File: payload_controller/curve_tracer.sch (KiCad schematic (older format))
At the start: 28 parts, among them U10 OPA2387, U12 ADS131M04IPWR, U13 INA190A4IDDFR, U31 LT6654AMPS6-1.25

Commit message: Continuing layout
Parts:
- removed U10: OPA2387, Package_SON:WSON-8-1EP_2x2mm_P0.5mm_EP0.9x1.6mm, symbol OPA2387:OPA2387
- added U10: OPA2387, Package_SON:WSON-8-1EP_2x2mm_P0.5mm_EP0.9x1.6mm, symbol OPA2387:OPA2387
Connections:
- net +3V3: now also U10.8
- net -3V3: now also U10.4
- net at R23.2: now also U10.1, U10.2 (-)
- net at R25.1: now also U10.3 (+)
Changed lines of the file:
@@
 $EndComp
-$Comp
-L OPA2387:OPA2387 U10
-U 2 1 6382B343
-P 7750 4550
-F 0 "U10" H 8000 4850 50  0000 C CNN
-F 1 "OPA2387" H 8100 4750 50  0000 C CNN
-F 2 "Package_SON:WSON-8-1EP_2x2mm_P0.5mm_EP0.9x1.6mm" H 8150 4750 50  0001 C CNN
-F 3 "" H 8150 4750 50  0001 C CNN
-	2    7750 4550
-	-1   0    0    -1
-$EndComp
-Connection ~ 7250 4550
 $Comp
 L power:-3V3 #PWR0151
 U 1 1 63853834
-P 8200 4750
-F 0 "#PWR0151" H 8200 4850 50  0001 C CNN
-F 1 "-3V3" H 8215 4923 50  0000 C CNN
-F 2 "" H 8200 4750 50  0001 C CNN
-F 3 "" H 8200 4750 50  0001 C CNN
-	1    8200 4750
+P 7650 4850
+F 0 "#PWR0151" H 7650 4950 50  0001 C CNN
+F 1 "-3V3" H 7665 5023 50  0000 C CNN
+F 2 "" H 7650 4850 50  0001 C CNN
+F 3 "" H 7650 4850 50  0001 C CNN
+	1    7650 4850
 	-1   0    0    1
 $EndComp
-Wire Wire Line
-	8000 4550 8200 4550
-Wire Wire Line
-	8200 4550 8200 4750
+$Comp
+L power:+3V3 #PWR0135
+U 1 1 63AD679A
+P 7650 4250
+F 0 "#PWR0135" H 7650 4100 50  0001 C CNN
+F 1 "+3V3" H 7665 4423 50  0000 C CNN
+F 2 "" H 7650 4250 50  0001 C CNN
+F 3 "" H 7650 4250 50  0001 C CNN
+	1    7650 4250
+	1    0    0    -1
+$EndComp
+$Comp
+L OPA2387:OPA2387 U?
+U 1 1 63AD4C17
+P 7750 4550
+AR Path="/635FEB2F/63AD4C17" Ref="U?"  Part="1"
+AR Path="/63C503EE/63AD4C17" Ref="U10"  Part="1"
+F 0 "U10" H 8100 4850 50  0000 R CNN
+F 1 "OPA2387" H 8300 4750 50  0000 R CNN
+F 2 "Package_SON:WSON-8-1EP_2x2mm_P0.5mm_EP0.9x1.6mm" H 8150 4750 50  0001 C CNN
+F 3 "" H 8150 4750 50  0001 C CNN
+	1    7750 4550
+	-1   0    0    -1
+$EndComp
 $EndSCHEMATC

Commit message: Continuing payload design
- Add OR gate for reverse bias
- Add GaAs panel connectors
- Add 3D models
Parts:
- added TP1: Current Test, Connector_PinHeader_2.54mm:PinHeader_1x02_P2.54mm_Vertical, symbol Connector:TestPoint_2Pole
- added TP2: Voltage Test+, Connector_PinHeader_2.54mm:PinHeader_1x01_P2.54mm_Vertical, symbol Connector:TestPoint
- added TP3: Voltage Test-, Connector_PinHeader_2.54mm:PinHeader_1x01_P2.54mm_Vertical, symbol Connector:TestPoint
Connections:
- net GND: now also TP3.1
- net PANEL_VOLTAGE: now also TP1.1; no longer R24.2, U13.7 (IN+)
- net at R25.2, R26.1, R27.2: now also TP2.1
- new net: R24.2, TP1.2, U13.7 (IN+)
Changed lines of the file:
@@
 Wire Wire Line
 	7450 2250 7450 2650
-Connection ~ 7450 2250
 Wire Wire Line
 	8450 2250 8450 4100
 Wire Wire Line
-	3300 2250 7450 2250
-Wire Wire Line
-	8450 5150 8450 4700
+	8450 5150 8450 4850
 Wire Wire Line
 	6400 4550 6950 4550
@@
 	-1   0    0    -1
 $EndComp
+$Comp
+L Connector:TestPoint TP?
+U 1 1 63A754DC
+P 8750 4400
+AR Path="/635FE71D/63A754DC" Ref="TP?"  Part="1"
+AR Path="/63C503EE/63A754DC" Ref="TP2"  Part="1"
+F 0 "TP2" V 8704 4588 50  0000 L CNN
+F 1 "Voltage Test+" V 8795 4588 50  0000 L CNN
+F 2 "Connector_PinHeader_2.54mm:PinHeader_1x01_P2.54mm_Vertical" H 8950 4400 50  0001 C CNN
+F 3 "~" H 8950 4400 50  0001 C CNN
+	1    8750 4400
+	0    1    1    0
+$EndComp
+Wire Wire Line
+	8750 4400 8450 4400
+$Comp
+L Connector:TestPoint_2Pole TP1
+U 1 1 63A77455
+P 6450 2250
+F 0 "TP1" H 6450 2445 50  0000 C CNN
+F 1 "Current Test" H 6450 2354 50  0000 C CNN
+F 2 "Connector_PinHeader_2.54mm:PinHeader_1x02_P2.54mm_Vertical" H 6450 2250 50  0001 C CNN
+F 3 "~" H 6450 2250 50  0001 C CNN
+	1    6450 2250
+	1    0    0    -1
+$EndComp
+Wire Wire Line
+	6650 2250 7450 2250
+Connection ~ 7450 2250
+Wire Wire Line
+	6250 2250 3300 2250
+$Comp
+L Connector:TestPoint TP?
+U 1 1 63A8A109
+P 8750 4850
+AR Path="/635FE71D/63A8A109" Ref="TP?"  Part="1"
+AR Path="/63C503EE/63A8A109" Ref="TP3"  Part="1"
+F 0 "TP3" V 8704 5038 50  0000 L CNN
+F 1 "Voltage Test-" V 8795 5038 50  0000 L CNN
+F 2 "Connector_PinHeader_2.54mm:PinHeader_1x01_P2.54mm_Vertical" H 8950 4850 50  0001 C CNN
+F 3 "~" H 8950 4850 50  0001 C CNN
+	1    8750 4850
+	0    1    1    0
+$EndComp
+Wire Wire Line
+	8750 4850 8450 4850
+Connection ~ 8450 4850
+Wire Wire Line
+	8450 4850 8450 4700
 $EndSCHEMATC

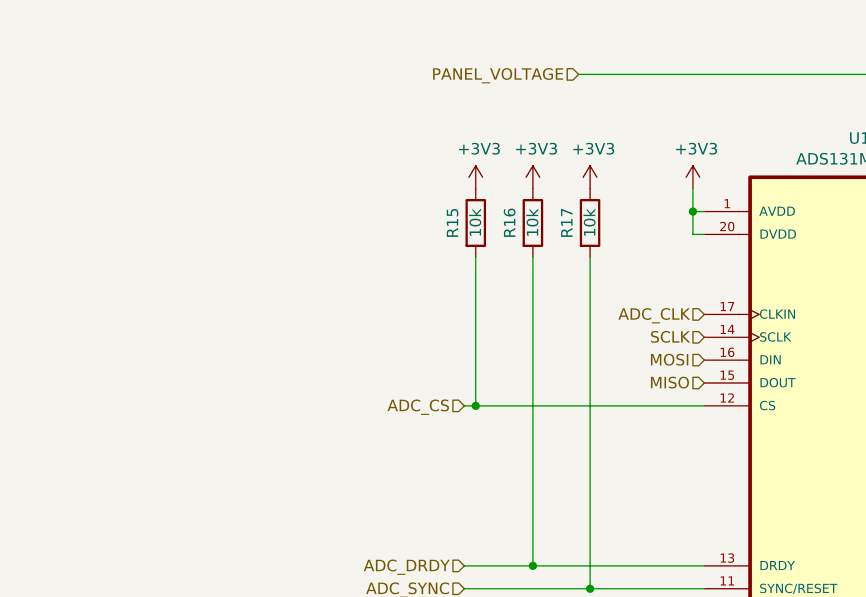
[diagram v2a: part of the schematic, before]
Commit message: Completed routing
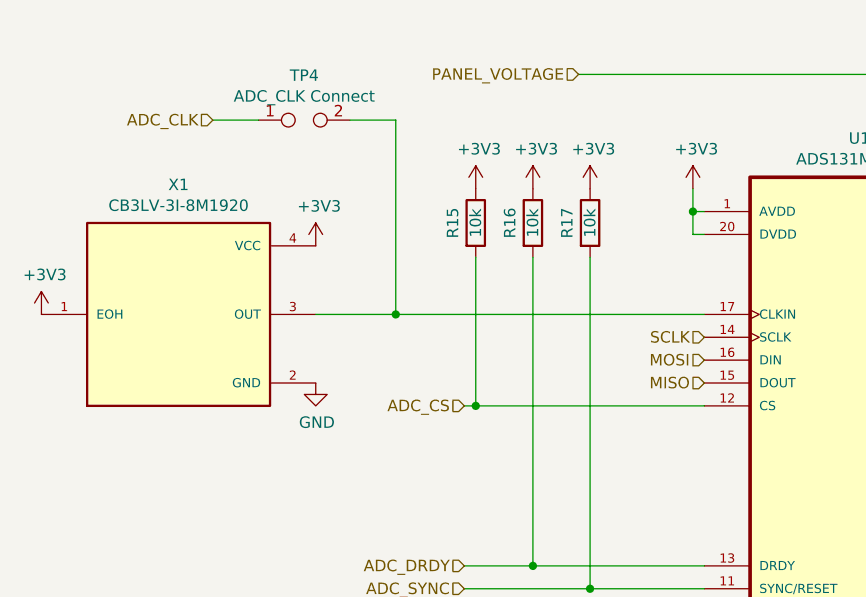
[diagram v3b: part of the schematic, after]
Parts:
- added TP4: ADC_CLK Connect, TestPoint:TestPoint_2Pads_Pitch2.54mm_Drill0.8mm, symbol Connector:TestPoint_2Pole
- added X1: CB3LV-3I-8M1920, CB3LV-3I-8M1920:OSCCC700X500X180-4N, symbol CB3LV-3I-8M1920:CB3LV-3I-8M1920
- TP1: footprint Connector_PinHeader_2.54mm:PinHeader_1x02_P2.54mm_Vertical -> TestPoint:TestPoint_2Pads_Pitch2.54mm_Drill0.8mm
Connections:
- net +3V3: now also X1.1 (EOH), X1.4 (VCC)
- net ADC_CLK: now also TP4.1; no longer U12.17 (CLKIN)
- net GND: now also X1.2 (GND)
- new net: TP4.2, U12.17 (CLKIN), X1.3 (OUT)
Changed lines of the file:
@@
 Text HLabel 2800 3700 0    50   Input ~ 0
 ADC_CS
-Text HLabel 3850 3300 0    50   Input ~ 0
+Text HLabel 1700 2450 0    50   Input ~ 0
 ADC_CLK
 Text HLabel 2800 4400 0    50   Input ~ 0
@@
 F 0 "TP1" H 6450 2445 50  0000 C CNN
 F 1 "Current Test" H 6450 2354 50  0000 C CNN
-F 2 "Connector_PinHeader_2.54mm:PinHeader_1x02_P2.54mm_Vertical" H 6450 2250 50  0001 C CNN
+F 2 "TestPoint:TestPoint_2Pads_Pitch2.54mm_Drill0.8mm" H 6450 2250 50  0001 C CNN
 F 3 "~" H 6450 2250 50  0001 C CNN
 	1    6450 2250
@@
 Wire Wire Line
 	8450 4850 8450 4700
+$Comp
+L CB3LV-3I-8M1920:CB3LV-3I-8M1920 X1
+U 1 1 6391FD82
+P 1550 3300
+F 0 "X1" H 1550 3867 50  0000 C CNN
+F 1 "CB3LV-3I-8M1920" H 1550 3776 50  0000 C CNN
+F 2 "CB3LV-3I-8M1920:OSCCC700X500X180-4N" H 1550 3300 50  0001 L BNN
+F 3 "" H 1550 3300 50  0001 L BNN
+F 4 "CTS Electronic Components" H 1550 3300 50  0001 L BNN "MANUFACTURER"
+	1    1550 3300
+	1    0    0    -1
+$EndComp
+$Comp
+L power:GND #PWR0141
+U 1 1 639207C4
+P 2150 3600
+F 0 "#PWR0141" H 2150 3350 50  0001 C CNN
+F 1 "GND" H 2155 3427 50  0000 C CNN
+F 2 "" H 2150 3600 50  0001 C CNN
+F 3 "" H 2150 3600 50  0001 C CNN
+	1    2150 3600
+	1    0    0    -1
+$EndComp
+$Comp
+L power:+3V3 #PWR0142
+U 1 1 63920C9B
+P 2150 3000
+F 0 "#PWR0142" H 2150 2850 50  0001 C CNN
+F 1 "+3V3" H 2165 3173 50  0000 C CNN
+F 2 "" H 2150 3000 50  0001 C CNN
+F 3 "" H 2150 3000 50  0001 C CNN
+	1    2150 3000
+	1    0    0    -1
+$EndComp
+Wire Wire Line
+	2150 3300 2500 3300
+Wire Wire Line
+	2500 2450 2500 3300
+Connection ~ 2500 3300
+Wire Wire Line
+	2500 3300 3850 3300
+$Comp
+L Connector:TestPoint_2Pole TP4
+U 1 1 63923F71
+P 2100 2450
+F 0 "TP4" H 2100 2645 50  0000 C CNN
+F 1 "ADC_CLK Connect" H 2100 2554 50  0000 C CNN
+F 2 "TestPoint:TestPoint_2Pads_Pitch2.54mm_Drill0.8mm" H 2100 2450 50  0001 C CNN
+F 3 "~" H 2100 2450 50  0001 C CNN
+	1    2100 2450
+	1    0    0    -1
+$EndComp
+Wire Wire Line
+	1900 2450 1700 2450
+Wire Wire Line
+	2300 2450 2500 2450
+$Comp
+L power:+3V3 #PWR0143
+U 1 1 63928C65
+P 950 3300
+F 0 "#PWR0143" H 950 3150 50  0001 C CNN
+F 1 "+3V3" H 965 3473 50  0000 C CNN
+F 2 "" H 950 3300 50  0001 C CNN
+F 3 "" H 950 3300 50  0001 C CNN
+	1    950  3300
+	1    0    0    -1
+$EndComp
 $EndSCHEMATC

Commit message: Generated manufacturing files
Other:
- moved on the sheet: C16, C20, C42
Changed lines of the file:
@@
 encoding utf-8
 Sheet 3 6
-Title ""
-Date ""
+Title "Curve Tracing Circuits"
+Date "2022-11-30"
 Rev "B"
 Comp "Advanced eXperimental Payloads | UNL Aerospace Club"
 Comment1 "Copyright (c) 2022"
 Comment2 "Designer: WSA"
-Comment3 "Reviewer:"
-Comment4 "Approved: "
+Comment3 "Reviewer: WSA"
+Comment4 "Approved: WSA"
 $EndDescr
 $Comp
@@
 L Device:C C?
 U 1 1 63CE93FD
-P 2900 7200
+P 950 7200
 AR Path="/6313FC31/63CE93FD" Ref="C?"  Part="1"
 AR Path="/63CE93FD" Ref="C?"  Part="1"
 AR Path="/635FE71D/63CE93FD" Ref="C?"  Part="1"
 AR Path="/63C503EE/63CE93FD" Ref="C16"  Part="1"
-F 0 "C16" V 3152 7200 50  0000 C CNN
-F 1 "0.1u" V 3061 7200 50  0000 C CNN
-F 2 "Capacitor_SMD:C_0603_1608Metric" H 2938 7050 50  0001 C CNN
-F 3 "~" H 2900 7200 50  0001 C CNN
-	1    2900 7200
+F 0 "C16" V 1202 7200 50  0000 C CNN
+F 1 "0.1u" V 1111 7200 50  0000 C CNN
+F 2 "Capacitor_SMD:C_0603_1608Metric" H 988 7050 50  0001 C CNN
+F 3 "~" H 950 7200 50  0001 C CNN
+	1    950  7200
 	1    0    0    -1
 $EndComp
@@
 L power:+3V3 #PWR?
 U 1 1 63CE9403
-P 2900 7050
+P 950 7050
 AR Path="/6313FC31/63CE9403" Ref="#PWR?"  Part="1"
 AR Path="/63CE9403" Ref="#PWR?"  Part="1"
 AR Path="/635FE71D/63CE9403" Ref="#PWR?"  Part="1"
 AR Path="/63C503EE/63CE9403" Ref="#PWR0149"  Part="1"
-F 0 "#PWR0149" H 2900 6900 50  0001 C CNN
-F 1 "+3V3" H 2915 7223 50  0000 C CNN
-F 2 "" H 2900 7050 50  0001 C CNN
-F 3 "" H 2900 7050 50  0001 C CNN
-	1    2900 7050
+F 0 "#PWR0149" H 950 6900 50  0001 C CNN
+F 1 "+3V3" H 965 7223 50  0000 C CNN
+F 2 "" H 950 7050 50  0001 C CNN
+F 3 "" H 950 7050 50  0001 C CNN
+	1    950  7050
 	1    0    0    -1
 $EndComp
@@
 L power:GND #PWR?
 U 1 1 63CE9409
-P 2900 7350
+P 950 7350
 AR Path="/6313FC31/63CE9409" Ref="#PWR?"  Part="1"
 AR Path="/63CE9409" Ref="#PWR?"  Part="1"
 AR Path="/635FE71D/63CE9409" Ref="#PWR?"  Part="1"
 AR Path="/63C503EE/63CE9409" Ref="#PWR0150"  Part="1"
-F 0 "#PWR0150" H 2900 7100 50  0001 C CNN
-F 1 "GND" H 2905 7177 50  0000 C CNN
-F 2 "" H 2900 7350 50  0001 C CNN
-F 3 "" H 2900 7350 50  0001 C CNN
-	1    2900 7350
+F 0 "#PWR0150" H 950 7100 50  0001 C CNN
+F 1 "GND" H 955 7177 50  0000 C CNN
+F 2 "" H 950 7350 50  0001 C CNN
+F 3 "" H 950 7350 50  0001 C CNN
+	1    950  7350
 	1    0    0    -1
 $EndComp
@@
 L power:+3V3 #PWR?
 U 1 1 63CEC86B
-P 4150 7050
+P 1350 7050
 AR Path="/6313FC31/63CEC86B" Ref="#PWR?"  Part="1"
 AR Path="/63CEC86B" Ref="#PWR?"  Part="1"
 AR Path="/635FE71D/63CEC86B" Ref="#PWR?"  Part="1"
 AR Path="/63C503EE/63CEC86B" Ref="#PWR0166"  Part="1"
-F 0 "#PWR0166" H 4150 6900 50  0001 C CNN
-F 1 "+3V3" H 4165 7223 50  0000 C CNN
-F 2 "" H 4150 7050 50  0001 C CNN
-F 3 "" H 4150 7050 50  0001 C CNN
-	1    4150 7050
+F 0 "#PWR0166" H 1350 6900 50  0001 C CNN
+F 1 "+3V3" H 1365 7223 50  0000 C CNN
+F 2 "" H 1350 7050 50  0001 C CNN
+F 3 "" H 1350 7050 50  0001 C CNN
+	1    1350 7050
 	1    0    0    -1
 $EndComp
@@
 L Device:C C?
 U 1 1 63CEC865
-P 4150 7200
+P 1350 7200
 AR Path="/6313FC31/63CEC865" Ref="C?"  Part="1"
 AR Path="/63CEC865" Ref="C?"  Part="1"
 AR Path="/635FE71D/63CEC865" Ref="C?"  Part="1"
 AR Path="/63C503EE/63CEC865" Ref="C20"  Part="1"
-F 0 "C20" V 4402 7200 50  0000 C CNN
-F 1 "1u" V 4311 7200 50  0000 C CNN
-F 2 "Capacitor_SMD:C_0603_1608Metric" H 4188 7050 50  0001 C CNN
-F 3 "~" H 4150 7200 50  0001 C CNN
-	1    4150 7200
+F 0 "C20" V 1602 7200 50  0000 C CNN
+F 1 "1u" V 1511 7200 50  0000 C CNN
+F 2 "Capacitor_SMD:C_0603_1608Metric" H 1388 7050 50  0001 C CNN
+F 3 "~" H 1350 7200 50  0001 C CNN
+	1    1350 7200
 	1    0    0    -1
 $EndComp
@@
 L power:GND #PWR?
 U 1 1 637C4863
-P 4550 7350
+P 1750 7350
 AR Path="/6313FC31/637C4863" Ref="#PWR?"  Part="1"
 AR Path="/637C4863" Ref="#PWR?"  Part="1"
 AR Path="/635FE71D/637C4863" Ref="#PWR?"  Part="1"
 AR Path="/63C503EE/637C4863" Ref="#PWR0245"  Part="1"
-F 0 "#PWR0245" H 4550 7100 50  0001 C CNN
-F 1 "GND" H 4555 7177 50  0000 C CNN
-F 2 "" H 4550 7350 50  0001 C CNN
-F 3 "" H 4550 7350 50  0001 C CNN
-	1    4550 7350
+F 0 "#PWR0245" H 1750 7100 50  0001 C CNN
+F 1 "GND" H 1755 7177 50  0000 C CNN
+F 2 "" H 1750 7350 50  0001 C CNN
+F 3 "" H 1750 7350 50  0001 C CNN
+	1    1750 7350
 	1    0    0    -1
 $EndComp
@@
 L power:+3V3 #PWR?
 U 1 1 637C4869
-P 4550 7050
+P 1750 7050
 AR Path="/6313FC31/637C4869" Ref="#PWR?"  Part="1"
 AR Path="/637C4869" Ref="#PWR?"  Part="1"
 AR Path="/635FE71D/637C4869" Ref="#PWR?"  Part="1"
 AR Path="/63C503EE/637C4869" Ref="#PWR0246"  Part="1"
-F 0 "#PWR0246" H 4550 6900 50  0001 C CNN
-F 1 "+3V3" H 4565 7223 50  0000 C CNN
-F 2 "" H 4550 7050 50  0001 C CNN
-F 3 "" H 4550 7050 50  0001 C CNN
-	1    4550 7050
+F 0 "#PWR0246" H 1750 6900 50  0001 C CNN
+F 1 "+3V3" H 1765 7223 50  0000 C CNN
+F 2 "" H 1750 7050 50  0001 C CNN
+F 3 "" H 1750 7050 50  0001 C CNN
+	1    1750 7050
 	1    0    0    -1
 $EndComp
@@
 L Device:C C?
 U 1 1 637C486F
-P 4550 7200
+P 1750 7200
 AR Path="/6313FC31/637C486F" Ref="C?"  Part="1"
 AR Path="/637C486F" Ref="C?"  Part="1"
 AR Path="/635FE71D/637C486F" Ref="C?"  Part="1"
 AR Path="/63C503EE/637C486F" Ref="C42"  Part="1"
-F 0 "C42" V 4802 7200 50  0000 C CNN
-F 1 "0.1u" V 4711 7200 50  0000 C CNN
-F 2 "Capacitor_SMD:C_0603_1608Metric" H 4588 7050 50  0001 C CNN
-F 3 "~" H 4550 7200 50  0001 C CNN
-	1    4550 7200
+F 0 "C42" V 2002 7200 50  0000 C CNN
+F 1 "0.1u" V 1911 7200 50  0000 C CNN
+F 2 "Capacitor_SMD:C_0603_1608Metric" H 1788 7050 50  0001 C CNN
+F 3 "~" H 1750 7200 50  0001 C CNN
+	1    1750 7200
 	1    0    0    -1
 $EndComp
@@
 L power:GND #PWR?
 U 1 1 63CEC871
-P 4150 7350
+P 1350 7350
 AR Path="/6313FC31/63CEC871" Ref="#PWR?"  Part="1"
 AR Path="/63CEC871" Ref="#PWR?"  Part="1"
 AR Path="/635FE71D/63CEC871" Ref="#PWR?"  Part="1"
 AR Path="/63C503EE/63CEC871" Ref="#PWR0165"  Part="1"
-F 0 "#PWR0165" H 4150 7100 50  0001 C CNN
-F 1 "GND" H 4155 7177 50  0000 C CNN
-F 2 "" H 4150 7350 50  0001 C CNN
-F 3 "" H 4150 7350 50  0001 C CNN
-	1    4150 7350
-	1    0    0    -1
-$EndComp
+F 0 "#PWR0165" H 1350 7100 50  0001 C CNN
+F 1 "GND" H 1355 7177 50  0000 C CNN
+F 2 "" H 1350 7350 50  0001 C CNN
+F 3 "" H 1350 7350 50  0001 C CNN
+	1    1350 7350
+	1    0    0    -1
+$EndComp
